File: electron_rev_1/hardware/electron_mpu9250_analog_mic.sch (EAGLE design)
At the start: 43 parts, among them IC2 S25FL128SAGNFI011, IC4 MIC_I2S_SPH0645, U1 MPU-9250, U10 GAS_SENSOR, U2 Value, U3 OPA322AIDBVT, U4 microSD, U5 +5v, U6 +5v, U7 GAS_SENSOR

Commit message: before ripping everything up and removing the timer
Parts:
- removed IC2: S25FL128SAGNFI011, S25FL128SAGNFI011:S25FL128SAGNFI011
- removed R3: 54.9K, resistor:R-US_R0603
- removed R4: 196K, resistor:R-US_R0603
- removed SJ1, SJ2: (no value), jumper:SJ
- removed U2: Value, TPL5010:TPL5010DDCR
- removed U6: +5v, SparkFun-IC-Power:V_REG_78XX7812
- removed U7: GAS_SENSOR, SparkFun:GAS_SENSOR
- added C10: 2.2uF, SparkFun-Capacitors:0.1UF-25V(+80/-20%)(0603)
- added C11: 220uF, SparkFun-Capacitors:0.1UF-25V(+80/-20%)(0603)
- added C12: 10uF, SparkFun-Capacitors:0.1UF-25V(+80/-20%)(0603)
- added C9: 4.7uF, SparkFun-Capacitors:0.1UF-25V(+80/-20%)(0603)
- added L2: 6.8uH, resistor:L-USL3225P
- added R18, R19, R20: 10K, resistor:R-US_R0603
- added R21, R22, R23, R24: (no value), resistor:R-US_R0603
- R17: value 10k -> (none)
- U5: value +5v -> TPS61030PWPR; device SparkFun-IC-Power:V_REG_78XX7812 -> TPS61030PWPR:TPS61030PWPR
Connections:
- removed net D6: U$5.6
- removed net H2: U6.OUT, U7.A1, U7.H1
- new net C_DET: R18.1, U$5.6, U4.CD1
- new net EN: U5.EN
- new net LBO: R24.1, U5.LBO
- new net N$12: R17.2, R21.1, U5.LBI
- net A1: no longer U2.RST_N
- net B1: now also R16.2, U10.B1
- net B2: no longer R16.2, U10.B1
- net B3: no longer R17.2, U7.B1
- net DAC: no longer U2.WAKE
- net GND: now also C10.2, C11.2, C12.2, C9.2, R23.1, U5.PGND, U5.PGND_2, U5.PGND_3, U5.SYNC; no longer IC2.VSS, R3.1, R4.1, U2.GND, U6.GND, U7.H2
- net H1: now also C10.1, C11.1, R22.2, R24.2, U5.VOUT, U5.VOUT_2, U5.VOUT_3; no longer U5.OUT
- net MISO: no longer IC2.SO/IO1
- net MOSI: now also R20.1; no longer IC2.SI/IO0
- net N$10: now also L2.2, U5.SW, U5.SW_2; no longer SJ1.1, SJ2.2, U5.IN
- net N$11: now also R22.1, R23.2, U5.FB; no longer SJ2.1, U6.IN
- net SCK: no longer IC2.SCK
- net SS: now also R19.1; no longer IC2.CS#
- net VBAT: now also C12.1, L2.1, R21.2, U5.VBAT; no longer SJ1.2
- net VCC: now also C9.1, R18.2, R19.2, R20.2; no longer IC2.VCC, R3.2, R4.2, U2.DELAY_M_RST, U2.VDD
- net WKP: no longer U2.DONE
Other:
- note added: "Add power cycle circuit"
- note added: "add to electron"
- note added: "check inductor footprint"
- note added: "expose unused pins"
- note added: "pick values"
- note added: "this is labeled strangly..."
- note removed: "CO Sensor"
- note removed: "MEM"
- note removed: "Memory."
- note removed: "TIMER"
- note removed: "USING SPI_0 because SS 1/2 required by I2S"
- note removed: "http://www.cypress.com/file/177966/download"
- moved on the sheet: R16, R17

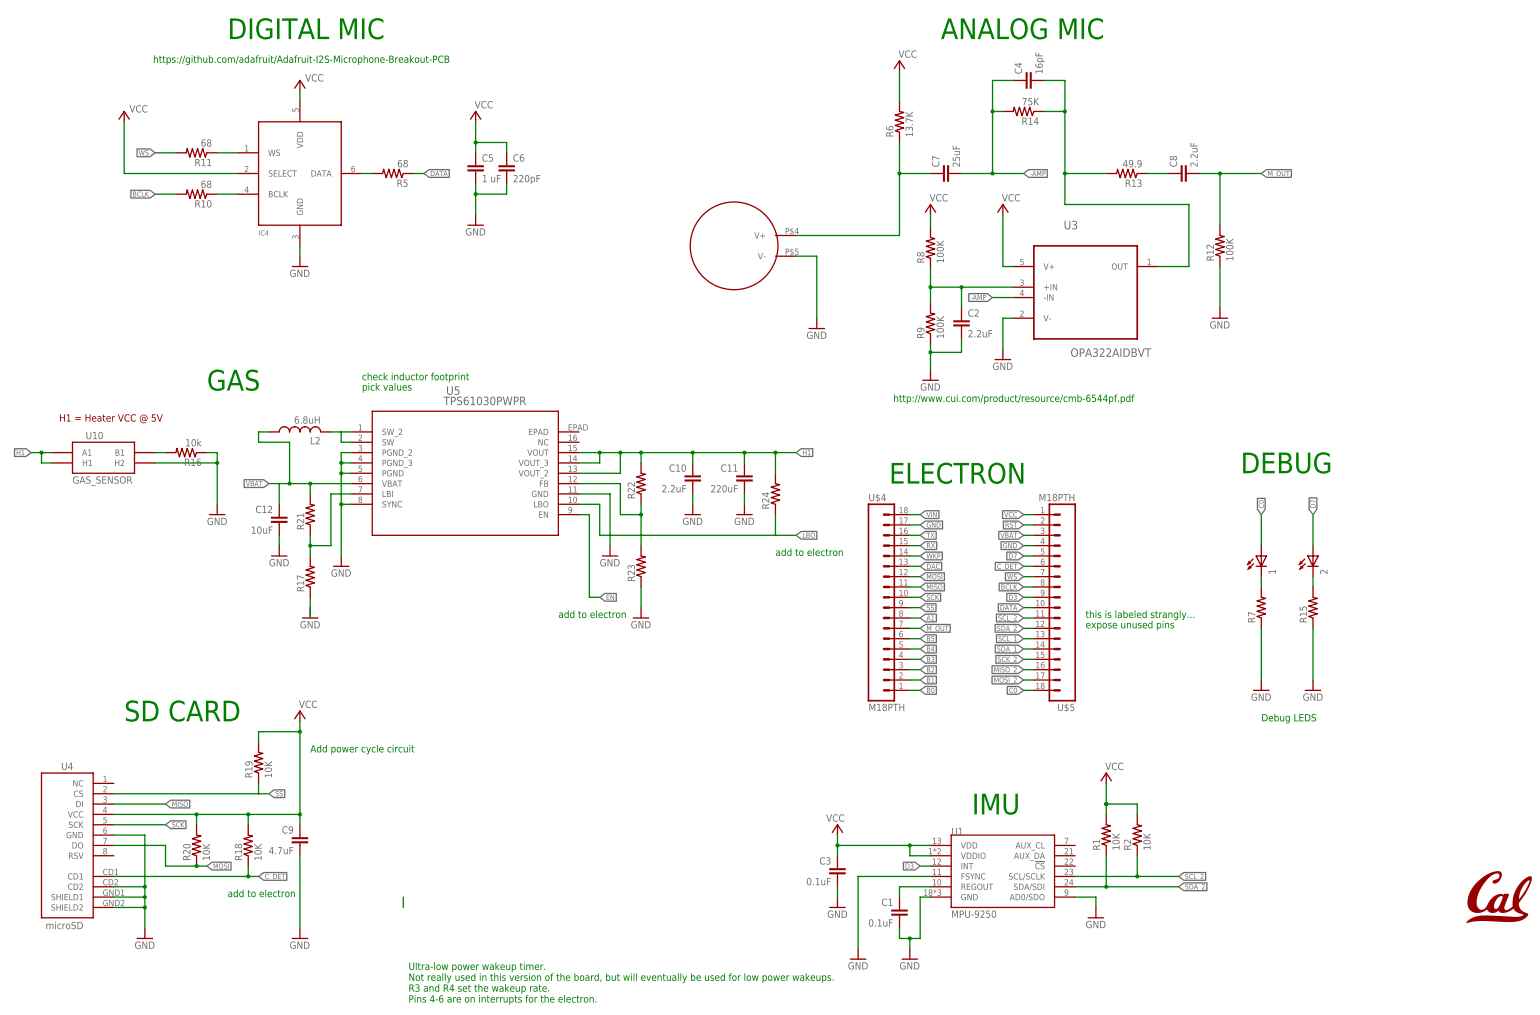
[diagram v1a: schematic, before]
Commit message: reroute with a single gas sensor
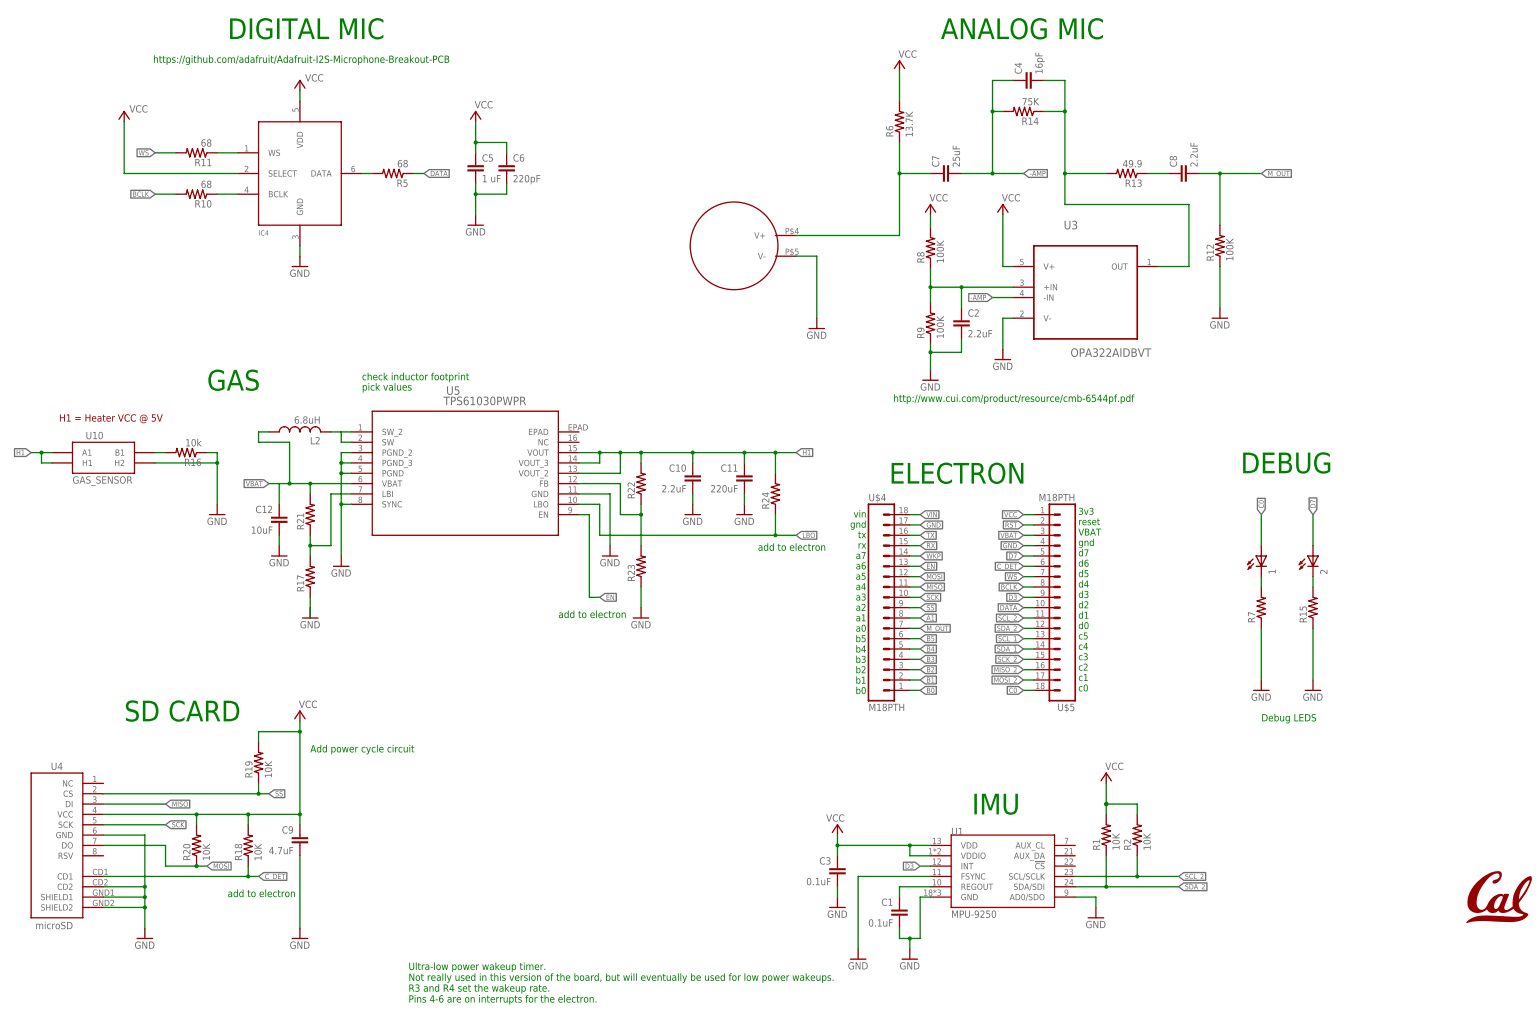
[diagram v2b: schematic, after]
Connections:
- removed net DAC: U$4.13
- net EN: now also U$4.13
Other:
- note added: "3v3 reset VBAT gnd d7 d6 d5 d4 d3 d2 d1 d0 c5 c4 c3 c2 c1 c0"
- note added: "vin gnd tx rx a7 a6 a5 a4 a3 a2 a1 a0 b5 b4 b3 b2 b1 b0"
- note removed: "expose unused pins"
- note removed: "this is labeled strangly..."
- moved on the sheet: U4
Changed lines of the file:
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@@
 <text x="-10.16" y="124.46" size="1.778" layer="91">pick values</text>
 <text x="-10.16" y="127" size="1.778" layer="91">check inductor footprint</text>
-<text x="167.64" y="68.58" size="1.778" layer="91">this is labeled strangly... </text>
-<text x="167.64" y="66.04" size="1.778" layer="91">expose unused pins</text>
 <text x="38.1" y="68.58" size="1.778" layer="91">add to electron</text>
-<text x="91.44" y="83.82" size="1.778" layer="91">add to electron</text>
+<text x="87.122" y="85.09" size="1.778" layer="91">add to electron</text>
 <text x="-43.18" y="0" size="1.778" layer="91">add to electron</text>
+<text x="165.862" y="50.546" size="1.7018" layer="91">3v3
+reset
+VBAT
+gnd
+d7
+d6
+d5
+d4
+d3
+d2
+d1
+d0
+c5
+c4
+c3
+c2
+c1
+c0</text>
+<text x="113.792" y="94.996" size="1.7018" layer="91" rot="R180">vin
+gnd
+tx
+rx
+a7
+a6
+a5
+a4
+a3
+a2
+a1
+a0
+b5
+b4
+b3
+b2
+b1
+b0</text>
 </plain>
 <instances>
@@
 <instance part="GND14" gate="1" x="223.52" y="50.8"/>
 <instance part="R15" gate="G$1" x="223.52" y="71.12" rot="R90"/>
-<instance part="U4" gate="G$1" x="-78.74" y="15.24" smashed="yes" rot="MR0">
-<attribute name="NAME" x="-84.074" y="31.242" size="1.778" layer="95"/>
-<attribute name="VALUE" x="-87.884" y="-7.874" size="1.778" layer="96"/>
+<instance part="U4" gate="G$1" x="-81.28" y="15.24" smashed="yes" rot="MR0">
+<attribute name="NAME" x="-86.614" y="31.242" size="1.778" layer="95"/>
+<attribute name="VALUE" x="-90.424" y="-7.874" size="1.778" layer="96"/>
 </instance>
 <instance part="U10" gate="G$1" x="-73.66" y="106.68"/>
@@
 </segment>
 <segment>
-<wire x1="-71.12" y1="15.24" x2="-63.5" y2="15.24" width="0.1524" layer="91"/>
-<wire x1="-71.12" y1="-2.54" x2="-63.5" y2="-2.54" width="0.1524" layer="91"/>
+<wire x1="-73.66" y1="15.24" x2="-63.5" y2="15.24" width="0.1524" layer="91"/>
+<wire x1="-73.66" y1="-2.54" x2="-63.5" y2="-2.54" width="0.1524" layer="91"/>
 <wire x1="-63.5" y1="-2.54" x2="-63.5" y2="0" width="0.1524" layer="91"/>
 <wire x1="-63.5" y1="0" x2="-63.5" y2="2.54" width="0.1524" layer="91"/>
 <wire x1="-63.5" y1="2.54" x2="-63.5" y2="15.24" width="0.1524" layer="91"/>
-<wire x1="-71.12" y1="0" x2="-63.5" y2="0" width="0.1524" layer="91"/>
+<wire x1="-73.66" y1="0" x2="-63.5" y2="0" width="0.1524" layer="91"/>
 <junction x="-63.5" y="0"/>
 <pinref part="U4" gate="G$1" pin="GND"/>
@@
 <pinref part="U4" gate="G$1" pin="SHIELD2"/>
 <pinref part="U4" gate="G$1" pin="CD2"/>
-<wire x1="-71.12" y1="2.54" x2="-63.5" y2="2.54" width="0.1524" layer="91"/>
+<wire x1="-73.66" y1="2.54" x2="-63.5" y2="2.54" width="0.1524" layer="91"/>
 <junction x="-63.5" y="2.54"/>
 <pinref part="GND19" gate="1" pin="GND"/>
@@
 </segment>
 </net>
-<net name="DAC" class="0">
-<segment>
-<pinref part="U$4" gate="G$1" pin="13"/>
-<wire x1="124.46" y1="81.28" x2="127" y2="81.28" width="0.1524" layer="91"/>
-<label x="127" y="81.28" size="1.27" layer="95" xref="yes"/>
-</segment>
-</net>
 <net name="MOSI" class="0">
 <segment>
@@
 </segment>
 <segment>
-<wire x1="-71.12" y1="12.7" x2="-58.42" y2="12.7" width="0.1524" layer="91"/>
+<wire x1="-73.66" y1="12.7" x2="-58.42" y2="12.7" width="0.1524" layer="91"/>
 <pinref part="U4" gate="G$1" pin="DO"/>
 <pinref part="R20" gate="G$1" pin="1"/>
@@
 </segment>
 <segment>
-<wire x1="-71.12" y1="22.86" x2="-58.42" y2="22.86" width="0.1524" layer="91"/>
+<wire x1="-73.66" y1="22.86" x2="-58.42" y2="22.86" width="0.1524" layer="91"/>
 <pinref part="U4" gate="G$1" pin="DI"/>
 <label x="-58.42" y="22.86" size="1.27" layer="95" xref="yes"/>
@@
 </segment>
 <segment>
-<wire x1="-71.12" y1="17.78" x2="-58.42" y2="17.78" width="0.1524" layer="91"/>
+<wire x1="-73.66" y1="17.78" x2="-58.42" y2="17.78" width="0.1524" layer="91"/>
 <pinref part="U4" gate="G$1" pin="SCK"/>
 <label x="-58.42" y="17.78" size="1.27" layer="95" xref="yes"/>
@@
 <pinref part="U4" gate="G$1" pin="CS"/>
 <pinref part="R19" gate="G$1" pin="1"/>
-<wire x1="-71.12" y1="25.4" x2="-35.56" y2="25.4" width="0.1524" layer="91"/>
+<wire x1="-73.66" y1="25.4" x2="-35.56" y2="25.4" width="0.1524" layer="91"/>
 <wire x1="-35.56" y1="25.4" x2="-35.56" y2="27.94" width="0.1524" layer="91"/>
 <wire x1="-35.56" y1="25.4" x2="-33.02" y2="25.4" width="0.1524" layer="91"/>
 <label x="-33.02" y="25.4" size="1.27" layer="95" xref="yes"/>
+<junction x="-35.56" y="25.4"/>
 </segment>
 </net>
@@
 </segment>
 <segment>
-<wire x1="-71.12" y1="20.32" x2="-50.8" y2="20.32" width="0.1524" layer="91"/>
+<wire x1="-73.66" y1="20.32" x2="-50.8" y2="20.32" width="0.1524" layer="91"/>
 <pinref part="U4" gate="G$1" pin="VCC"/>
 <pinref part="P+6" gate="VCC" pin="VCC"/>
@@
 <segment>
 <pinref part="U4" gate="G$1" pin="CD1"/>
-<wire x1="-71.12" y1="5.08" x2="-38.1" y2="5.08" width="0.1524" layer="91"/>
+<wire x1="-73.66" y1="5.08" x2="-38.1" y2="5.08" width="0.1524" layer="91"/>
 <label x="-35.56" y="5.08" size="1.27" layer="95" xref="yes"/>
 <pinref part="R18" gate="G$1" pin="1"/>
@@
 <wire x1="91.44" y1="88.9" x2="96.52" y2="88.9" width="0.1524" layer="91"/>
 <label x="96.52" y="88.9" size="1.27" layer="95" xref="yes"/>
+<junction x="91.44" y="88.9"/>
 </segment>
 </net>
@@
 <label x="48.26" y="73.66" size="1.27" layer="95" xref="yes"/>
 </segment>
-</net>
-<net name="N$13" class="0">
-<segment>
-<wire x1="0" y1="0" x2="0" y2="-2.54" width="0.1524" layer="91"/>
-</segment>
-</net>
+<segment>
+<pinref part="U$4" gate="G$1" pin="13"/>
+<wire x1="124.46" y1="81.28" x2="127" y2="81.28" width="0.1524" layer="91"/>
+<label x="127" y="81.28" size="1.27" layer="95" xref="yes"/>
+</segment>
+</net>

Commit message: ugh, rewire w out gas sensor. need to add fet for power cycling the sd card and then will ship
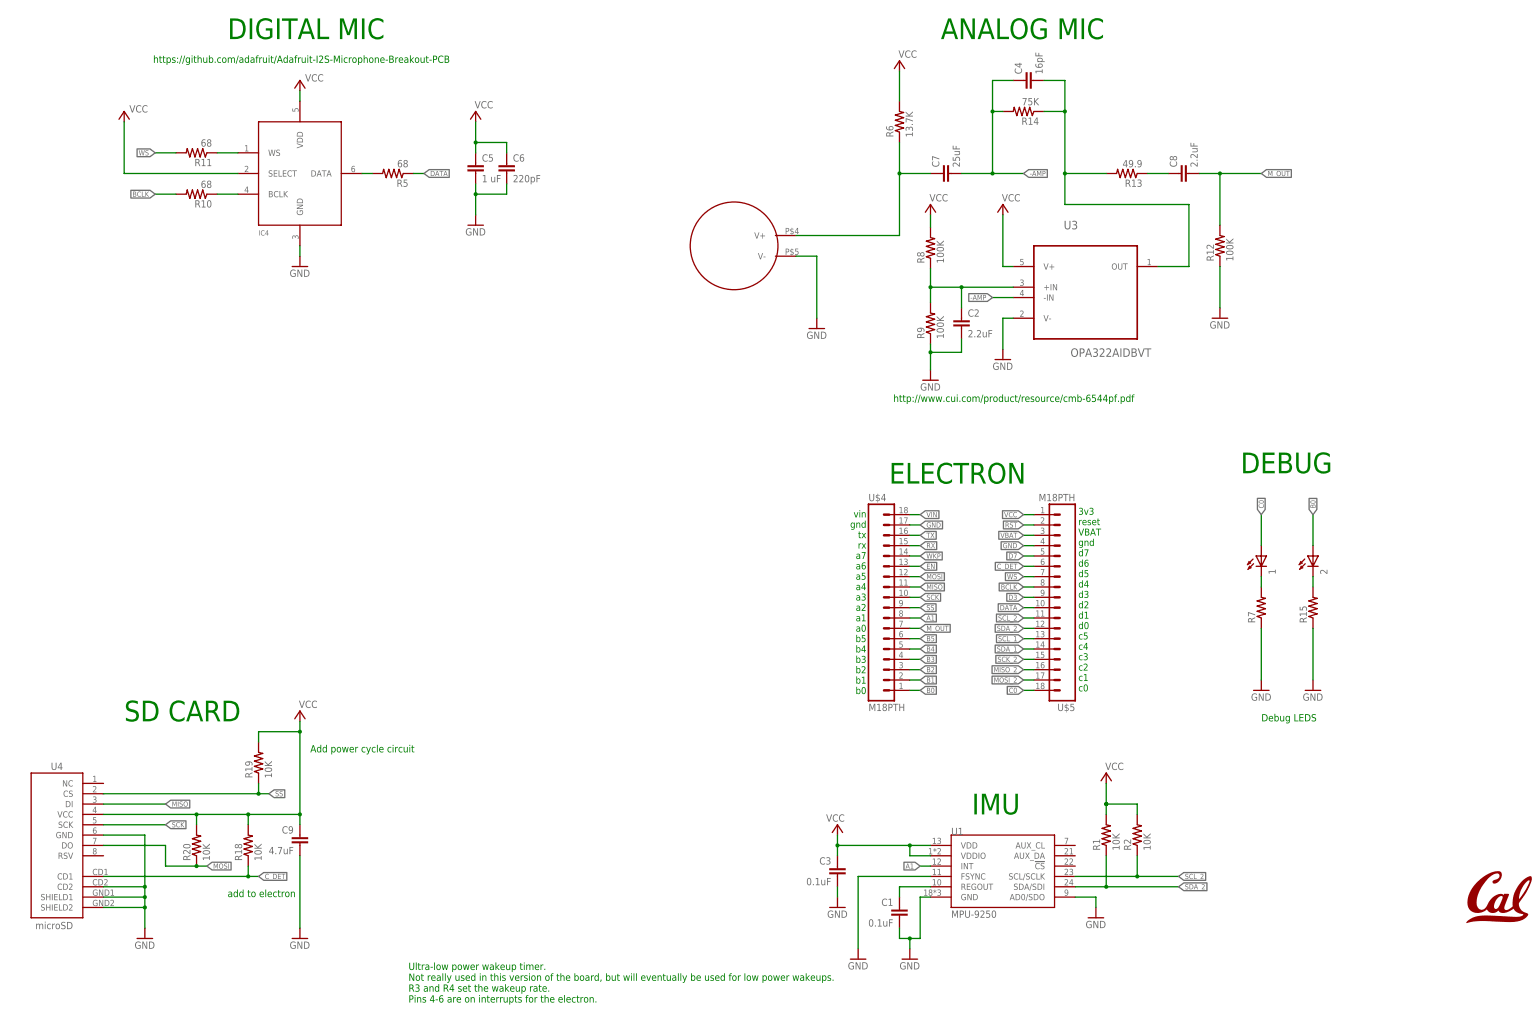
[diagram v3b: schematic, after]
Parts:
- removed C10: 2.2uF, SparkFun-Capacitors:0.1UF-25V(+80/-20%)(0603)
- removed C11: 220uF, SparkFun-Capacitors:0.1UF-25V(+80/-20%)(0603)
- removed C12: 10uF, SparkFun-Capacitors:0.1UF-25V(+80/-20%)(0603)
- removed L2: 6.8uH, resistor:L-USL3225P
- removed R16: 10k, resistor:R-US_R0603
- removed R17, R21, R22, R23, R24: (no value), resistor:R-US_R0603
- removed U10: GAS_SENSOR, SparkFun:GAS_SENSOR
- removed U5: TPS61030PWPR, TPS61030PWPR:TPS61030PWPR
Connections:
- removed net H1: C10.1, C11.1, R22.2, R24.2, U10.A1, U10.H1, U5.VOUT, U5.VOUT_2, U5.VOUT_3
- removed net LBO: R24.1, U5.LBO
- removed net N$10: L2.2, U5.SW, U5.SW_2
- removed net N$11: R22.1, R23.2, U5.FB
- removed net N$12: R17.2, R21.1, U5.LBI
- net A1: now also U1.INT
- net B0: now also 2.A
- net B1: no longer R16.2, U10.B1
- net D3: no longer U1.INT
- net D7: no longer 2.A
- net EN: no longer U5.EN
- net GND: no longer C10.2, C11.2, C12.2, R16.1, R17.1, R23.1, U10.H2, U5.GND, U5.PGND, U5.PGND_2, U5.PGND_3, U5.SYNC
- net VBAT: no longer C12.1, L2.1, R21.2, U5.VBAT
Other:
- note removed: "GAS"
- note removed: "H1 = Heater VCC @ 5V"
- note removed: "check inductor footprint"
- note removed: "pick values"
